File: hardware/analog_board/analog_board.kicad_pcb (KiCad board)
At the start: 4 copper layers, 212.3 x 151.4 mm, 331 parts, among them J1 2x5 牛角座, J2 Conn_02x08_Counter_Clockwise, J3 Conn_01x04_Pin, J4 Conn_01x08, J5 CH1, J6 CH1, Q1 MMBT3906, Q2 MMBT3906, U1 GW2A-LV18EQ144, U10 TPS54360DDA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

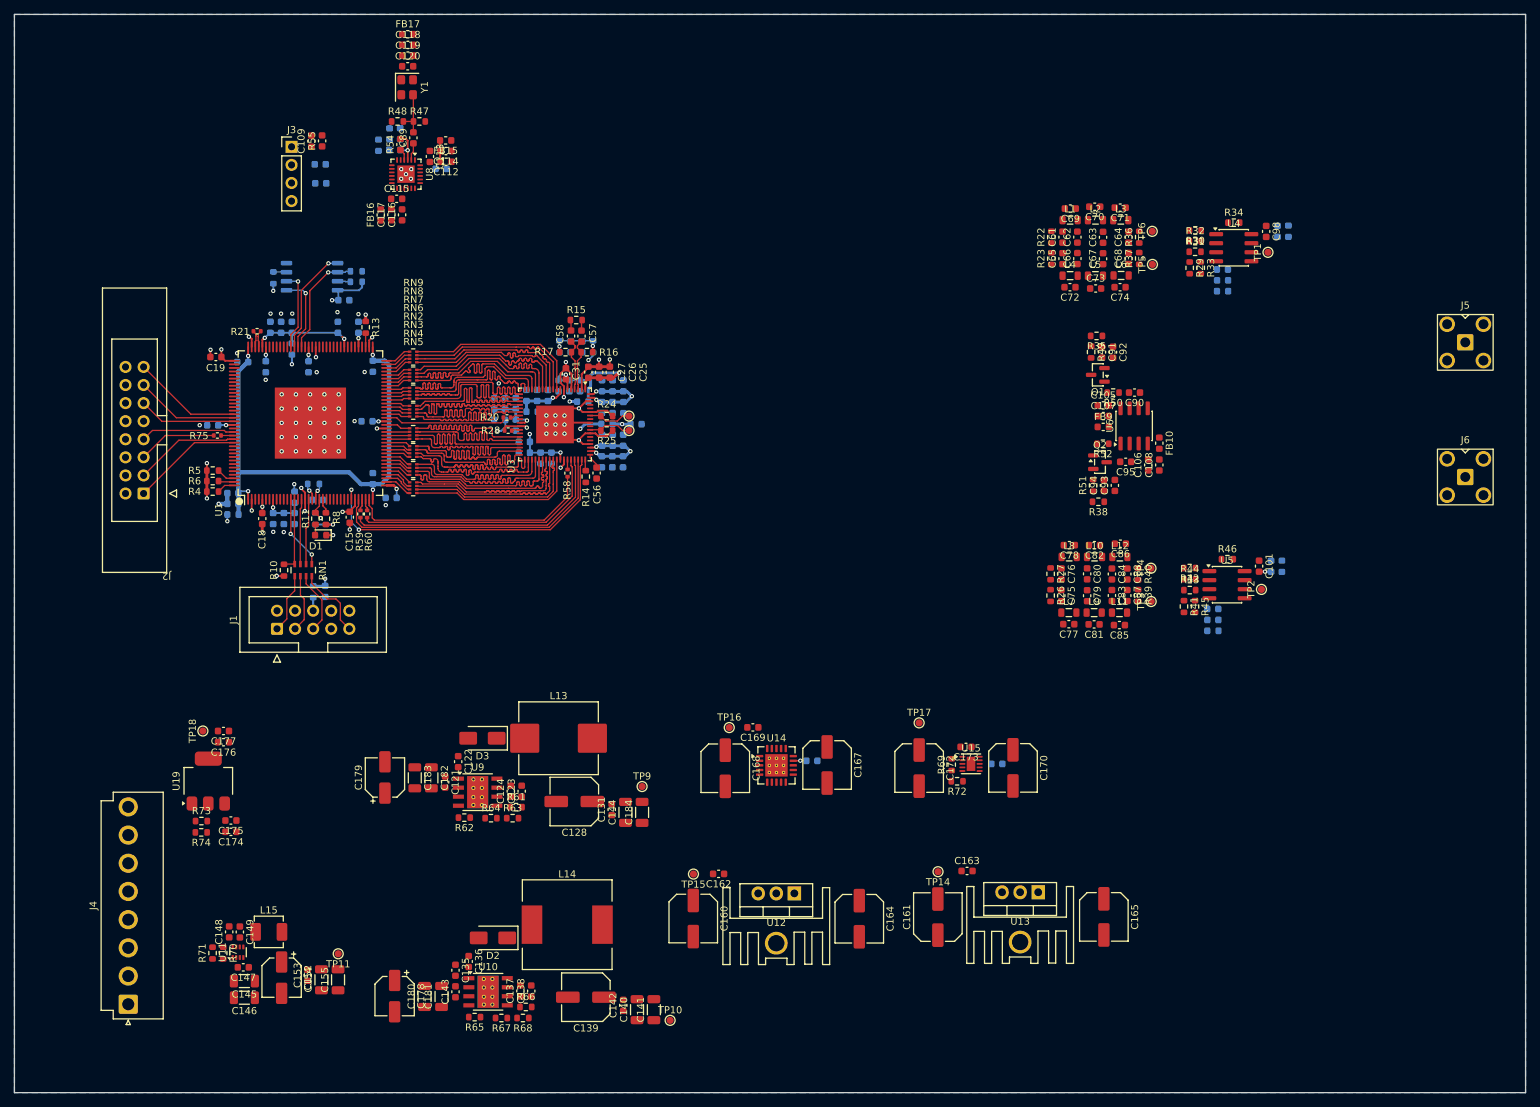
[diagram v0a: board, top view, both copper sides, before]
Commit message: feat：时钟电路布线
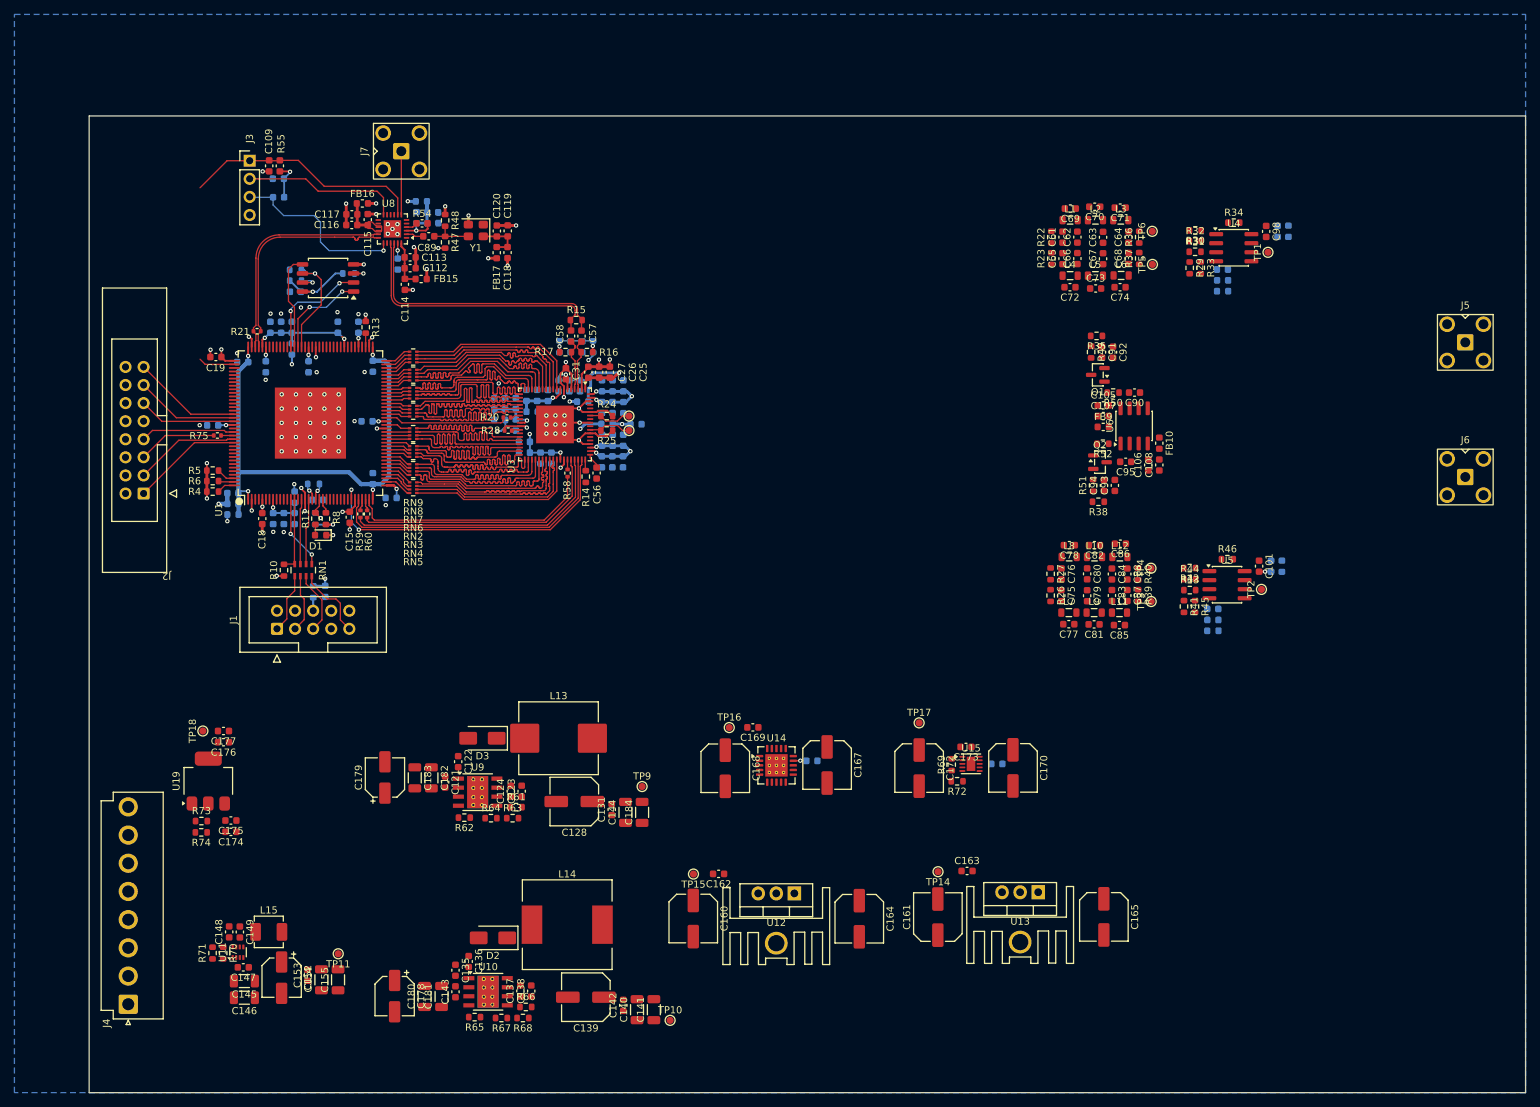
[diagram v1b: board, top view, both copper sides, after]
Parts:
- added J7: CH1, Connector_Coaxial:SMA_BAT_Wireless_BWSMA-KWE-Z001, F.Cu at (70.8, 31.2)
- U2: moved to F.Cu
- moved FB17 33.1 mm to (84.2, 45.5), turned to 90 degrees
- moved C118 32.4 mm to (85.8, 45.5), turned to 90 degrees
- moved C119 28.3 mm to (85.8, 42.4), turned to -90 degrees
- moved C120 26.3 mm to (84.3, 42.4), turned to -90 degrees
- moved Y1 22.3 mm to (81.3, 42.4), turned to 180 degrees
- moved FB15 19.8 mm to (73.6, 49.2)
- moved C114 19.6 mm to (71.3, 49.9), turned to 90 degrees
- moved R47 17.4 mm to (77.0, 44.0), turned to -90 degrees
- moved C112 15.8 mm to (72.1, 47.7)
- moved R48 15.4 mm to (77.0, 41.0), turned to -90 degrees
- moved R53 14.7 mm to (70.3, 47.1), turned to 90 degrees
- moved C113 14.4 mm to (72.1, 46.1), turned to 180 degrees
- moved C89 14.0 mm to (74.7, 43.2), turned to 0 degrees
- moved C110 13.4 mm to (75.3, 41.3), turned to 180 degrees
- moved C97 12.6 mm to (75.2, 39.8), turned to 180 degrees
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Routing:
- net +3.3VA: track 3.23 -> 71.6 mm, vias 1 -> 5
- net Clock_V_{DD}: track 5.30 -> 46.8 mm, vias 1 -> 3
- net /Clock/RESET_N: track 0.00 -> 39.1 mm
- net /Clock/DAC_CLK+: track 1.52 -> 37.5 mm
- net /Clock/DAC_CLK-: track 1.51 -> 37.5 mm
- net /Clock/FPGA_CLK-: track 2.39 -> 31.8 mm
- net /Clock/FPGA_CLK+: track 2.39 -> 31.7 mm
- net /Clock/SCL: track 0.00 -> 25.6 mm
- net /Clock/SDA: track 0.00 -> 25.3 mm, vias 0 -> 1
- net GND: track 69.6 -> 86.5 mm, vias 78 -> 89
- net /Clock/10MHz_OUT: track 0.00 -> 8.96 mm
- net Clock_V_{TCXO}: track 0.00 -> 6.47 mm
- net /FPGA_Config/MSPI_MI: track 11.2 -> 15.8 mm, vias 1 -> 2
- net Clock_V_{DDIO}: track 0.00 -> 4.48 mm
- net Clock_V_{VCO}: track 3.02 -> 6.73 mm
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- added copper zone on F.Cu, net Clock_V_{DDIO}
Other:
- board size 212.3 x 151.4 mm -> 201.8 x 137.2 mm

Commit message: feat：重构滤波器布局，共模反馈布局
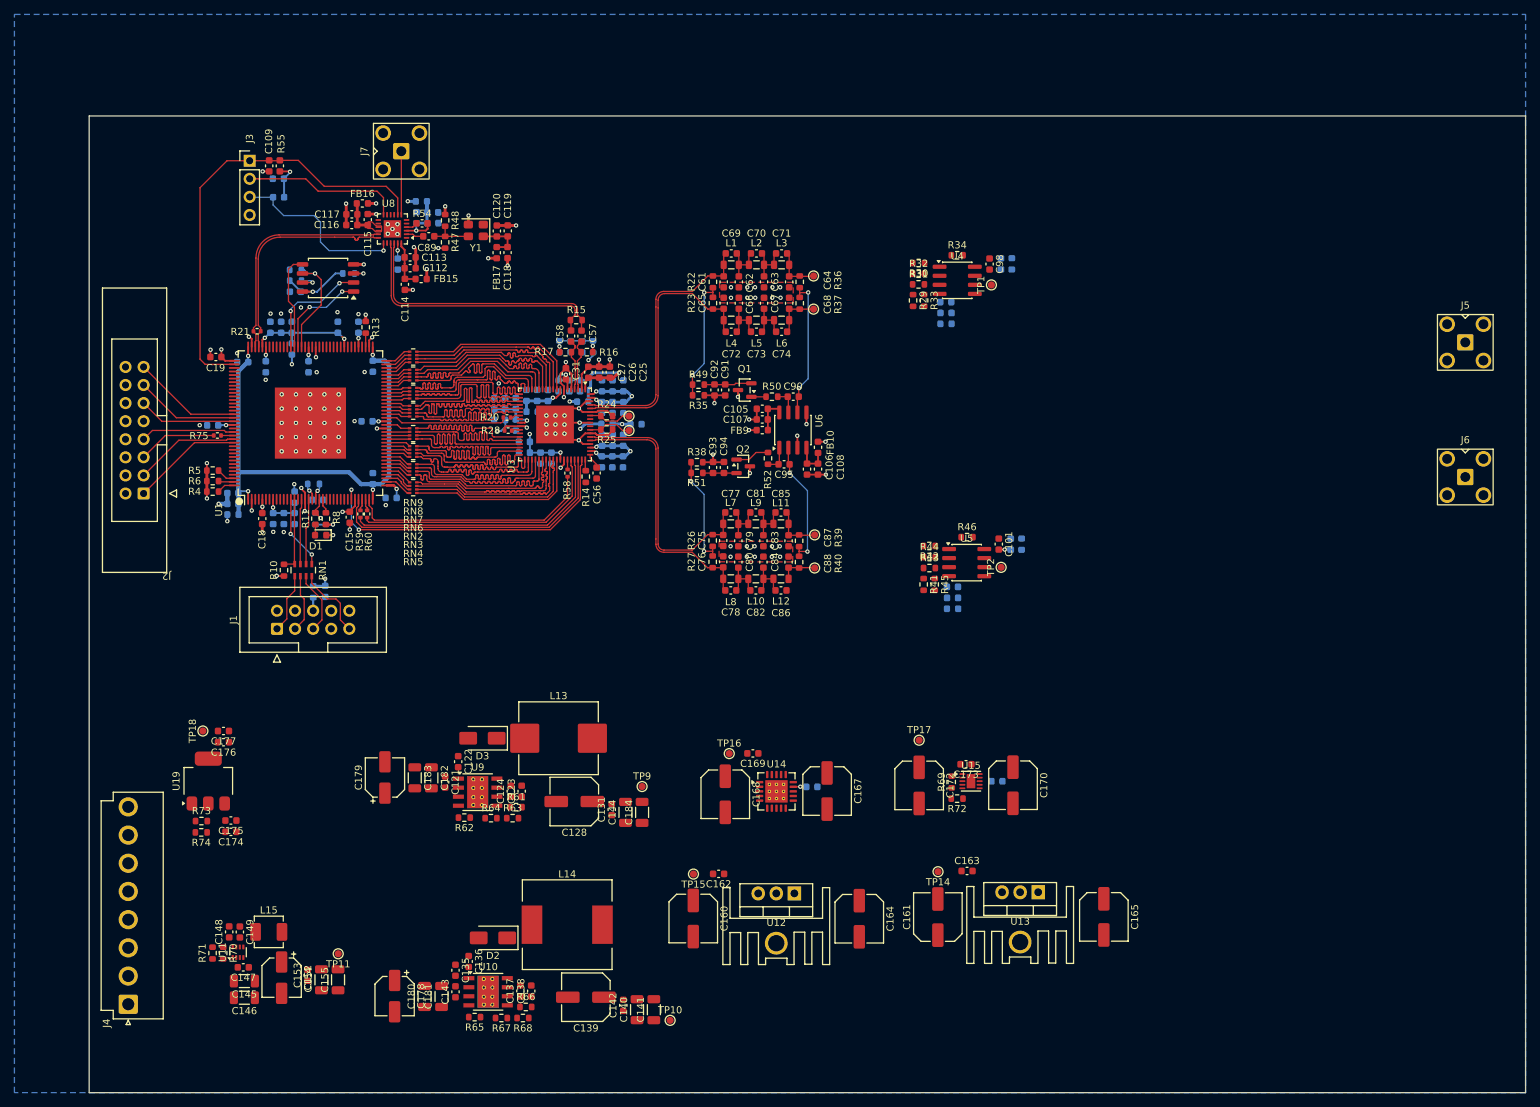
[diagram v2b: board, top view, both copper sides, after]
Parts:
- moved R38 56.7 mm to (112.4, 74.9)
- moved R35 56.5 mm to (112.6, 65.5)
- moved C93 56.5 mm to (114.6, 75.7), turned to -90 degrees
- moved C92 56.2 mm to (114.8, 64.8), turned to 90 degrees
- moved R51 55.7 mm to (112.4, 76.4), turned to 0 degrees
- moved R49 55.3 mm to (112.6, 64.0), turned to 0 degrees
- moved C94 53.4 mm to (116.2, 75.7), turned to -90 degrees
- moved C91 53.2 mm to (116.3, 64.8), turned to 90 degrees
- moved Q2 50.1 mm to (118.9, 75.5)
- moved C85 50.1 mm to (124.2, 82.0)
- moved C81 50.0 mm to (120.6, 82.0)
- moved C77 50.0 mm to (117.1, 82.0)
- moved Q1 49.6 mm to (119.1, 64.8)
- moved C79 49.6 mm to (118.2, 86.0), turned to 90 degrees
- moved C83 49.6 mm to (121.7, 86.0), turned to 90 degrees
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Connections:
- net Net-(U3-IOUT1N) renamed /DAC/IOUT1_N
- net Net-(U3-IOUT1P) renamed /DAC/IOUT1_P
- net Net-(U3-IOUT2N) renamed /DAC/IOUT2_N
- net Net-(U3-IOUT2P) renamed /DAC/IOUT2_P
- R41 pad 1: Net-(C85-Pad1) -> Net-(C86-Pad1)
- R42 pad 2: Net-(C86-Pad1) -> Net-(C85-Pad1)
- R43 pad 1: Net-(C85-Pad1) -> Net-(C86-Pad1)
- R44 pad 1: Net-(C86-Pad1) -> Net-(C85-Pad1)
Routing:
- net /DAC/IOUT1_N: track 0.00 -> 37.9 mm
- net /DAC/IOUT1_P: track 0.00 -> 37.8 mm
- net /DAC/IOUT2_N: track 0.00 -> 37.7 mm
- net /DAC/IOUT2_P: track 0.00 -> 37.7 mm
- net /Clock/RESET_N: track 39.1 -> 63.2 mm
- net Net-(U6B--): track 0.00 -> 20.0 mm, vias 0 -> 2
- net Net-(U6A--): track 0.00 -> 18.3 mm, vias 0 -> 2
- net Net-(R22-Pad1): track 0.00 -> 17.7 mm, vias 0 -> 2
- net GND: track 86.5 -> 103.0 mm, vias 89 -> 115
- net Net-(R26-Pad1): track 0.00 -> 15.8 mm, vias 0 -> 2
- net Net-(C85-Pad1): track 0.00 -> 7.01 mm
- net Net-(C68-Pad1): track 0.00 -> 6.86 mm
- net Net-(C64-Pad2): track 0.00 -> 6.80 mm
- net Net-(Q1-E): track 0.00 -> 6.68 mm
- net Net-(C66-Pad1): track 0.00 -> 6.50 mm
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- added copper zone on F.Cu, net GND

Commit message: feat：差分转单端电路布线
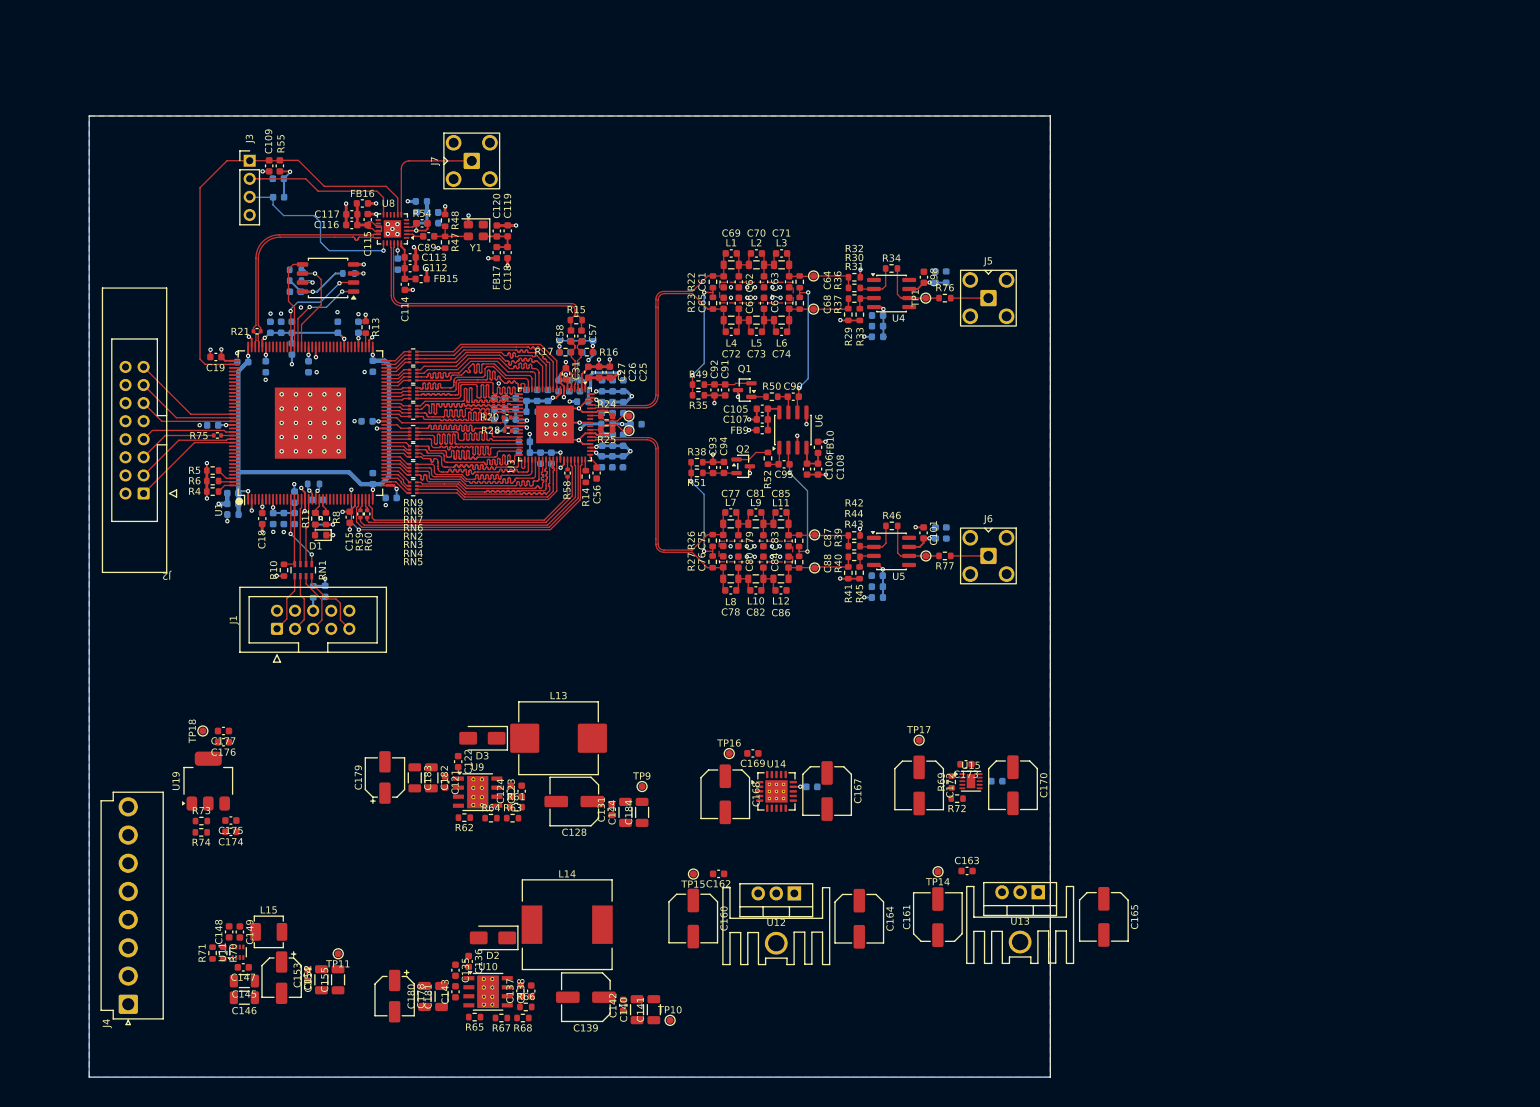
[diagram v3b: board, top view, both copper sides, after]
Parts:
- added R76: 49.9R, Resistor_SMD:R_0603_1608Metric, F.Cu at (147.2, 51.9)
- added R77: 49.9R, Resistor_SMD:R_0603_1608Metric, F.Cu at (147.2, 88.1)
- moved J6 67.9 mm to (153.3, 88.1)
- moved J5 67.3 mm to (153.3, 51.9)
- moved R41 10.7 mm to (133.6, 90.5)
- moved TP2 10.7 mm to (144.5, 88.1)
- moved C102 10.7 mm to (137.7, 90.9)
- moved C104 10.7 mm to (137.7, 92.4)
- moved FB8 10.7 mm to (137.7, 93.9)
- moved R43 10.7 mm to (134.5, 88.2)
- moved R46 10.7 mm to (139.7, 83.9)
- moved C101 10.7 mm to (144.2, 84.8)
- moved C103 10.7 mm to (145.9, 84.9)
- moved FB7 10.7 mm to (147.4, 84.9)
- moved U5 10.7 mm to (139.7, 87.5)
- moved R45 10.7 mm to (135.2, 90.5)
- moved R44 10.7 mm to (134.5, 86.7)
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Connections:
- J5 pad 1: /DAC/OUT1 -> Net-(J5-In)
- J6 pad 1: /DAC/OUT2 -> Net-(J6-In)
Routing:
- net /DAC/OUT2: track 0.00 -> 9.78 mm
- net /DAC/OUT1: track 0.00 -> 9.70 mm
- net GND: track 103.0 -> 111.7 mm, vias 115 -> 120
- net /Clock/10MHz_OUT: track 8.96 -> 16.9 mm
- net Net-(C64-Pad2): track 6.80 -> 13.3 mm
- net Net-(U5--): track 0.00 -> 6.32 mm
- net Net-(C86-Pad1): track 5.26 -> 11.6 mm
- net Net-(C68-Pad1): track 6.86 -> 13.2 mm
- net Net-(U4--): track 0.00 -> 6.26 mm
- net Net-(C85-Pad1): track 7.01 -> 13.3 mm
- net Net-(U4-V+): track 0.00 -> 5.58 mm, vias 0 -> 1
- net Net-(U4-V-): track 0.00 -> 5.52 mm, vias 0 -> 1
- net Net-(U5-V-): track 0.00 -> 5.49 mm, vias 0 -> 1
- net Net-(J6-In): track 0.00 -> 5.29 mm
- net Net-(J5-In): track 0.00 -> 5.29 mm
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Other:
- board size 201.8 x 137.2 mm -> 135 x 135 mm

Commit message: feat：电源布线完成
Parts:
- moved C170 96.5 mm to (61.1, 107.4), turned to 0 degrees
- moved C171 94.5 mm to (60.6, 109.7), turned to -90 degrees
- moved C173 92.0 mm to (58.2, 114.0), turned to -90 degrees
- moved U15 90.5 mm to (60.5, 113.3), turned to 90 degrees
- moved TP17 89.0 mm to (54.8, 120.6), turned to 90 degrees
- moved R69 87.6 mm to (60.7, 116.2), turned to 180 degrees
- moved R72 86.2 mm to (63.0, 115.2), turned to -90 degrees
- moved C172 82.4 mm to (61.1, 120.6), turned to 0 degrees
- moved R67 49.9 mm to (132.1, 136.8), turned to 0 degrees
- moved C165 48.2 mm to (130.0, 111.0), turned to 90 degrees
- moved C143 48.2 mm to (122.7, 130.1), turned to -90 degrees
- moved C164 48.1 mm to (96.1, 110.9)
- moved L14 47.5 mm to (138.8, 123.7)
- moved C140 47.5 mm to (148.6, 135.6)
- moved D2 47.5 mm to (128.3, 125.5)
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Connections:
- C152 pad 1: +1.0V -> +1V0
- C153 pad 2: +1.0V -> +1V0
- C154 pad 2: +1.0V -> +1V0
- C155 pad 2: +1.0V -> +1V0
- L15 pad 2: +1.0V -> +1V0
- R70 pad 2: +1.0V -> +1V0
- TP11 pad 1: +1.0V -> +1V0
- U14 pad 17: (no net) -> GND
- U14 pad 18: (no net) -> GND
- U14 pad 19: (no net) -> GND
- U14 pad 2: (no net) -> +3.3VA
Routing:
- net +1.8VA: track 10.00 -> 92.1 mm, vias 2 -> 4
- net +1V0: track 37.7 -> 89.9 mm, vias 3 -> 8
- net +3.3VA: track 71.6 -> 123.1 mm, vias 5 -> 10
- net +1.8VD: track 0.00 -> 36.4 mm, vias 0 -> 3
- net +7V: track 0.00 -> 22.4 mm, vias 0 -> 2
- net GND: track 111.7 -> 131.9 mm, vias 120 -> 268
- net +3.3V: track 44.2 -> 59.4 mm, vias 14 -> 16
- net +1.8VD_DAC: track 22.6 -> 28.9 mm
- net Net-(D3-K): track 0.00 -> 5.51 mm, vias 0 -> 2
- net Net-(D2-K): track 0.00 -> 5.37 mm, vias 0 -> 2
- net +5VA: track 1.08 -> 6.20 mm, vias 1 -> 11
- net Net-(U19-ADJ): track 0.00 -> 4.26 mm
- net Net-(U9-COMP): track 0.00 -> 3.46 mm
- net Net-(U15-FB): track 0.00 -> 3.40 mm
- net Net-(U10-COMP): track 0.00 -> 3.35 mm
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- added copper zone on F.Cu, net +1.8VA
- added copper zone on In2.Cu, net +1.8VA
- added copper zone on F.Cu, net +1.8VD
- added copper zone on In2.Cu, net +1.8VD
- added copper zone on F.Cu, net +17V
- added copper zone on B.Cu, net +1V0
- added copper zone on F.Cu, net +1V0
- added copper zone on In2.Cu, net +1V0
- added copper zone on F.Cu, net +3.3V
- added copper zone on B.Cu, net +3.3VA
- added copper zone on F.Cu, net +3.3VA
- added copper zone on In2.Cu, net +3.3VA
- added copper zone on F.Cu, net +5VA
- added copper zone on In2.Cu, net +5VA
- added copper zone on F.Cu, net +7V
- added copper zone on In2.Cu, net -17V
- added copper zone on F.Cu, net -5VA
- added copper zone on In2.Cu, net -5VA
- added copper zone on B.Cu, net -7V
- added copper zone on F.Cu, net -7V
- added copper zone on In2.Cu, net -7V
- added copper zone on F.Cu, net Net-(D2-K)
- added copper zone on F.Cu, net Net-(D3-K)
- added copper zone on F.Cu, net Net-(U11-SW)
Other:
- board size 135 x 135 mm -> 135 x 115 mm
